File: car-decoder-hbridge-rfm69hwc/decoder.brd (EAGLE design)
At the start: 98.7 x 80 mm, 50 parts, among them U1 RFM69HCW, U3 MCP73831, U4 ATMEGA328P, U6 MIC5219 3.3V, Y1 16MHZ

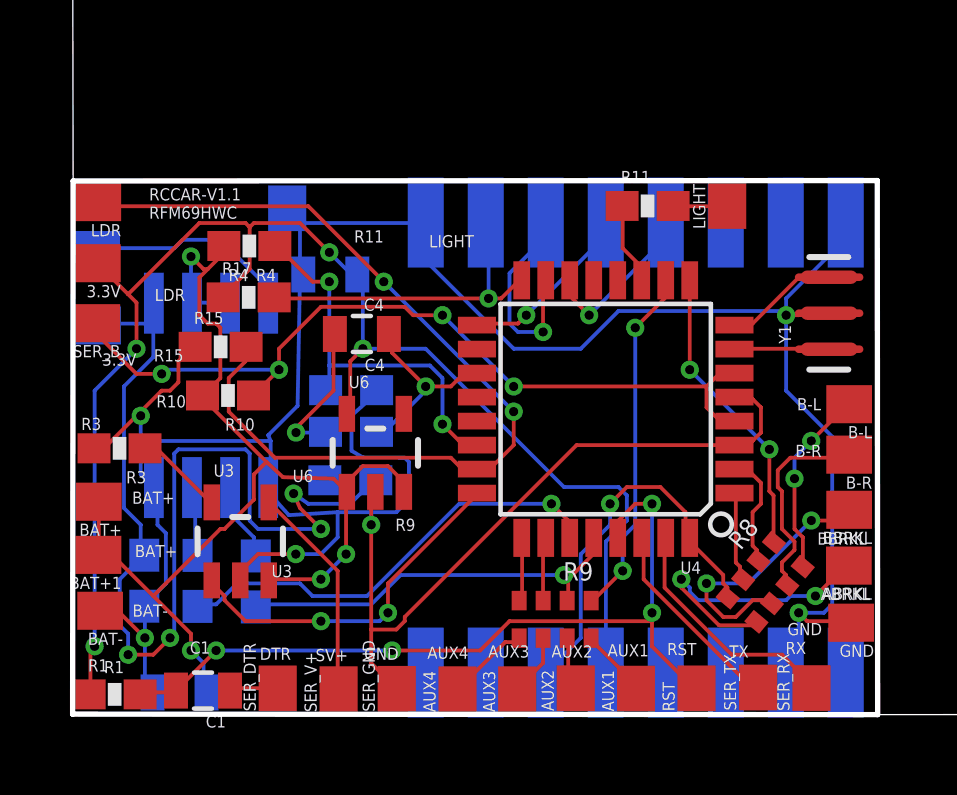
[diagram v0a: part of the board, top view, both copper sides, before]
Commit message: Fix boards and add the pi control station
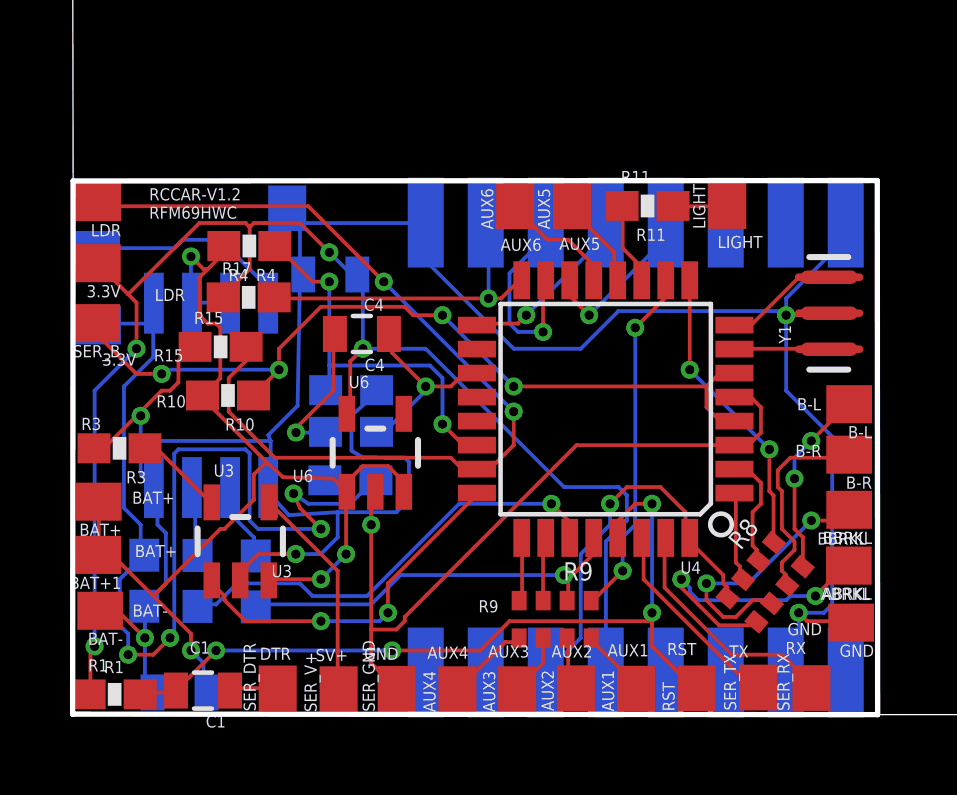
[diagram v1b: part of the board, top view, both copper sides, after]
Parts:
- added AUX5, AUX6: (no value), wirepad:SMD1,27-2,54
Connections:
- new net D8: AUX5.1, U4.12
- new net D9: AUX6.1, U4.13
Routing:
- net D9: track 0.00 -> 3.94 mm
- net D8: track 0.00 -> 3.10 mm
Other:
- board text added: "AUX5"
- board text added: "AUX6"
- board text added: "RCCAR-V1.2 RFM69HWC"
- board text removed: "2.56V"
- board text removed: "RCCAR-V1.1 RFM69HWC"
- board text removed: "VJ"
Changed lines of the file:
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@@
 <text x="13.881196875" y="16.57355" size="0.4064" layer="122" rot="MR90">gnd</text>
 <text x="17.853475" y="0.245521875" size="0.4064" layer="122" rot="MR90">rst</text>
-<text x="10.7455" y="15.694815625" size="0.4064" layer="121">R11</text>
+<text x="20.146646875" y="15.7491625" size="0.4064" layer="121">R11</text>
 <text x="5.272140625" y="1.99011875" size="0.4064" layer="121">C1</text>
 <text x="25.119665625" y="1.97890625" size="0.4064" layer="121">RX</text>
@@
 <text x="26.1853" y="5.622746875" size="0.4064" layer="121">BBRKL</text>
 <text x="25.4519125" y="8.5461" size="0.4064" layer="121">B-R</text>
-<text x="13.2416125" y="15.5344625" size="0.4064" layer="121">LIGHT</text>
+<text x="22.86013125" y="15.5072875" size="0.4064" layer="121">LIGHT</text>
 <text x="6.559878125" y="14.4072875" size="0.4064" layer="121">R4</text>
 <text x="11.073725" y="13.418803125" size="0.4064" layer="121">C4</text>
 <text x="8.69646875" y="7.71245625" size="0.4064" layer="121">U6</text>
-<text x="12.11916875" y="6.082940625" size="0.4064" layer="121">R9</text>
+<text x="14.89060625" y="3.365596875" size="0.4064" layer="121">R9</text>
 <text x="4.06999375" y="11.7311125" size="0.4064" layer="121">R15</text>
 <text x="4.15235625" y="10.1966625" size="0.4064" layer="121">R10</text>
@@
 <text x="2.34829375" y="11.58969375" size="0.4064" layer="121">3.3V</text>
 <text x="4.09765625" y="13.74605625" size="0.4064" layer="121">LDR</text>
-<text x="9.782278125" y="0.69541875" size="0.4064" layer="122" rot="MR0">2.56V</text>
 <text x="5.2804125" y="1.662365625" size="0.4064" layer="122" rot="MR0">C2</text>
-<text x="7.086275" y="2.2840625" size="0.4064" layer="122" rot="MR0">R6</text>
-<text x="5.44875" y="2.32046875" size="0.4064" layer="122" rot="MR0">R7</text>
+<text x="7.955746875" y="2.338409375" size="0.4064" layer="122" rot="MR0">R6</text>
+<text x="6.15519375" y="2.4291625" size="0.4064" layer="122" rot="MR0">R7</text>
 <text x="10.100234375" y="8.28173125" size="0.4064" layer="122" rot="MR0">R2</text>
 <text x="10.93001875" y="13.342371875" size="0.4064" layer="122" rot="MR0">R13</text>
-<text x="11.35748125" y="16.33940625" size="0.4064" layer="122" rot="MR0">GND</text>
-<text x="7.55603125" y="15.460175" size="0.4064" layer="122" rot="MR0">VJ</text>
-<text x="5.21449375" y="15.643503125" size="0.4064" layer="122" rot="MR0">VJ</text>
+<text x="10.54235" y="17.018740625" size="0.4064" layer="122" rot="MR0">GND</text>
 <text x="3.684240625" y="16.497009375" size="0.4064" layer="122" rot="MR0">MOTOR</text>
 <text x="3.589715625" y="13.82110625" size="0.4064" layer="122" rot="MR0">MT-GND</text>
@@
 <text x="9.358403125" y="11.35626875" size="0.4064" layer="122" rot="MR0">R5</text>
 <text x="6.539046875" y="10.655528125" size="0.4064" layer="122" rot="MR0">MDRIVER</text>
-<text x="3.912253125" y="16.488490625" size="0.4064" layer="121">RCCAR-V1.1
+<text x="3.912253125" y="16.488490625" size="0.4064" layer="121">RCCAR-V1.2
 RFM69HWC</text>
-<text x="7.16049375" y="16.543884375" size="0.4064" layer="122" rot="MR0">RCCAR-V1.1
+<text x="7.16049375" y="16.543884375" size="0.4064" layer="122" rot="MR0">RCCAR-V1.2
 RFM69HWC</text>
+<text x="17.58159375" y="15.45079375" size="0.4064" layer="121">AUX5</text>
+<text x="15.624853125" y="15.418175" size="0.4064" layer="121">AUX6</text>
 </plain>
 <attributes>
@@
 <element name="U1" library="SparkFun-RF" package="RFM69HCW-XXXS2" value="RFM69HCW" x="20.13378125" y="8.8597125" rot="MR270"/>
 <element name="R17" library="SparkFun-Resistors" package="0603-RES" value="10k" x="7.23198125" y="13.866196875"/>
+<element name="AUX5" library="wirepad" package="SMD1,27-2,54" value="" x="18.0090125" y="16.897565625"/>
+<element name="AUX6" library="wirepad" package="SMD1,27-2,54" value="" x="16.11595625" y="16.897565625"/>
 </elements>
 <signals>
@@
 <via x="8.809028125" y="9.3599" extent="1-16" drill="0.3048"/>
 </signal>
+<signal name="D8">
+<contactref element="U4" pad="12"/>
+<contactref element="AUX5" pad="1"/>
+<wire x1="19.4183" y1="15.367" x2="19.4183" y2="14.5288" width="0.127" layer="1"/>
+<wire x1="18.0213" y1="16.764" x2="19.4183" y2="15.367" width="0.127" layer="1"/>
+<wire x1="19.4183" y1="14.5288" x2="19.532634375" y2="14.434625" width="0.127" layer="1"/>
+<wire x1="18.0213" y1="16.764" x2="18.0090125" y2="16.897565625" width="0.127" layer="1"/>
+</signal>
+<signal name="D9">
+<contactref element="U4" pad="13"/>
+<contactref element="AUX6" pad="1"/>
+<wire x1="18.7198" y1="14.9479" x2="18.7198" y2="14.5288" width="0.127" layer="1"/>
+<wire x1="17.8816" y1="15.7861" x2="18.7198" y2="14.9479" width="0.127" layer="1"/>
+<wire x1="17.1831" y1="15.7861" x2="17.8816" y2="15.7861" width="0.127" layer="1"/>
+<wire x1="16.2052" y1="16.764" x2="17.1831" y2="15.7861" width="0.127" layer="1"/>
+<wire x1="18.7198" y1="14.5288" x2="18.732634375" y2="14.434625" width="0.127" layer="1"/>
+<wire x1="16.2052" y1="16.764" x2="16.11595625" y2="16.897565625" width="0.127" layer="1"/>
+</signal>
 </signals>
